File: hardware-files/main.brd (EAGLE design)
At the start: 62.2 x 70.8 mm, 27 parts, among them IC3 E73_2G4M04S, J4 SCREWTERMINAL_3X, Q1 BUZ11, Q2 BUZ11, Q3 BUZ11, Q4 BUZ11

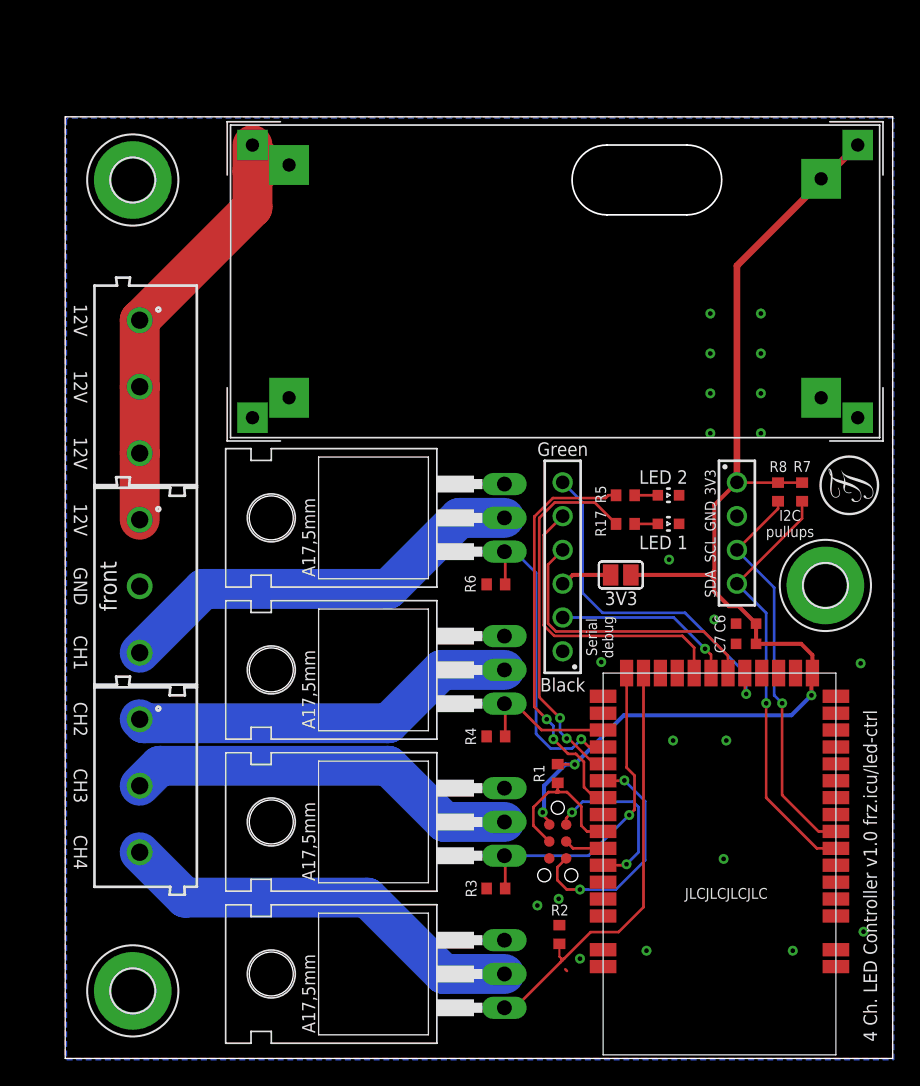
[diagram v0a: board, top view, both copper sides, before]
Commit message: added dc barrel jack
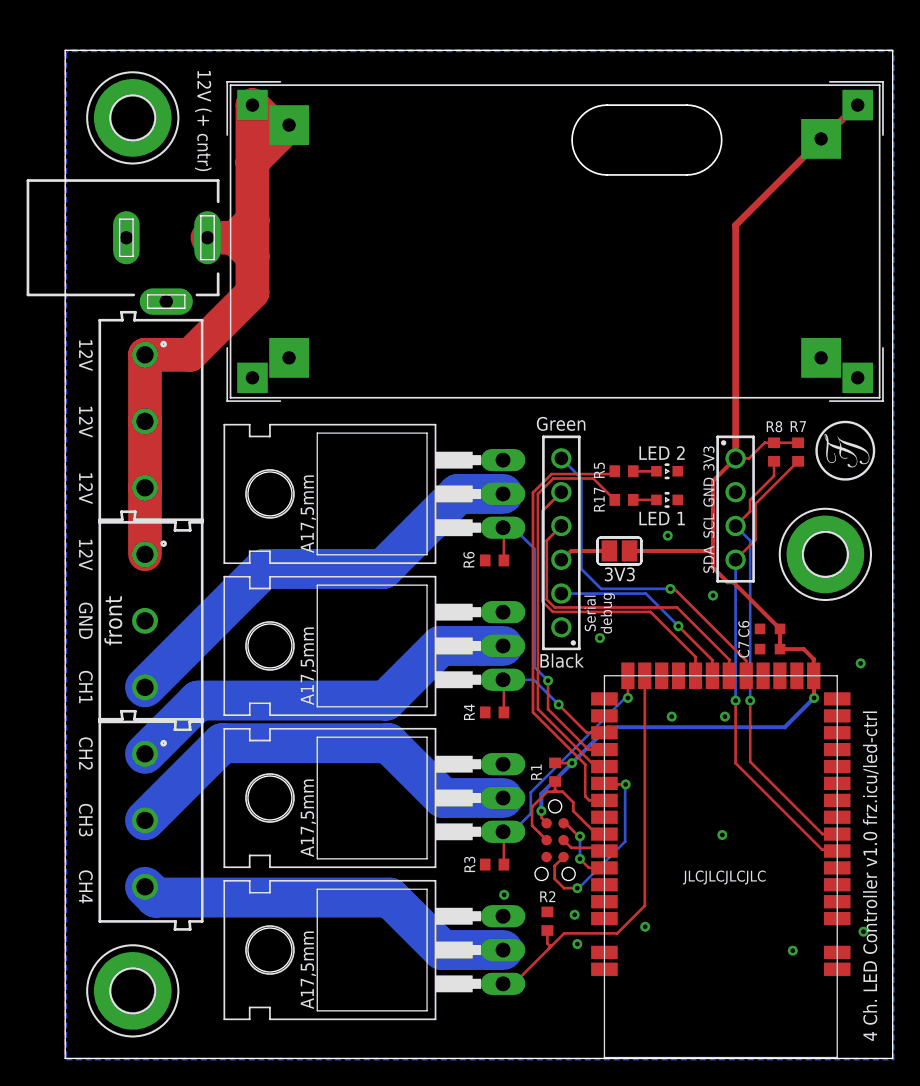
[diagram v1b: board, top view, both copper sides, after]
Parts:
- added J3: DCJ0202, con-jack:DCJ0202
- moved H3 4.67 mm to (5.08, 70.7)
- moved R8 3.01 mm to (53.3, 45.6)
- moved R7 3.01 mm to (55.1, 45.6)
- moved U$1 3.00 mm to (36.8, 61.4)
- moved J4 2.63 mm to (6.00, 32.9)
- moved H2 2.34 mm to (57.1, 37.9)
- moved C7 1.84 mm to (53.0, 30.8)
- moved C6 1.84 mm to (53.0, 32.3)
- moved D3 1.80 mm to (45.2, 42.0)
- moved R17 1.80 mm to (42.0, 42.0)
- moved Q1 1.80 mm to (26.6, 8.15)
- moved Q3 1.80 mm to (26.6, 31.0)
- moved R3 1.80 mm to (32.3, 14.6)
- moved R4 1.80 mm to (32.3, 26.0)
- moved D2 1.80 mm to (45.2, 44.1)
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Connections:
- net +12V: now also J3.1
- net GND: now also J3.3
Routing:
- net +12V: track 40.7 -> 52.2 mm
- net SWDIO: track 13.1 -> 5.46 mm
- net FET3: track 24.2 -> 18.6 mm
- net SCL: track 30.0 -> 33.0 mm
- net SDA: track 32.0 -> 35.0 mm
- net SWO: track 18.0 -> 15.0 mm
- net +3V3: track 90.6 -> 93.4 mm
- net CH4: track 31.2 -> 28.9 mm
- net N$20: track 27.9 -> 30.2 mm, vias 2 -> 0
- net N$21: track 30.8 -> 32.9 mm, vias 2 -> 0
- net RTS: track 26.9 -> 25.3 mm
- net CH1: track 31.6 -> 32.9 mm
- net CH3: track 29.8 -> 31.0 mm
- net FET2: track 10.7 -> 11.9 mm, vias 0 -> 1
- net CH2: track 29.2 -> 30.3 mm
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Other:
- board size 62.2 x 70.8 mm -> 62.2 x 75.8 mm
- board text added: "12V (+ cntr)"
- board text removed: "I2C pullups"
